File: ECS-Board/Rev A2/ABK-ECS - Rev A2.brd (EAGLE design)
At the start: 100 x 80 mm, 246 parts, among them J1 22-27-2061-06, J10 22-05-7068-06, J2 USB-B-S-RA, J3 1241050-5, J4 MSTBA2, J5 22-05-7068-06, J6 22-05-7028-02, J7 22-05-7068-06, J8 22-05-7068-06, J9 22-05-7028-02, K1 G6K-2G-Y, SW1 B3FS-1015, SW2 B3FS-1015, T1 EXMACHINA-LOGO-NAME, T10 MMBT2222AL, T11 MMBT2222AL, T12 IRLML5103TRPBF, T13 IRLML5103TRPBF, T14 IRLML5103TRPBF, T15 IRLML5103TRPBF, T16 MMBT2222AL, T17 MMBT2222AL, T18 MMBT2222AL, T19 MMBT2222AL, T2 IRLML5103TRPBF, T3 MMBT2222AL, T4 IRLML5103TRPBF, T5 IRLML5103TRPBF, T6 IRLML5103TRPBF, T7 IRLML5103TRPBF, T8 MMBT2222AL, T9 MMBT2222AL, U1 AT24C512C-SSHM-B, U2 LPC1768FBD100, U3 LT3686HDDPBF, U4 LT3686HDDPBF, U5 TC1264-3.3, U6 CD4050BD, U7 CD4050BD, X1 FC-135, X2 ASE-12, X3 3000

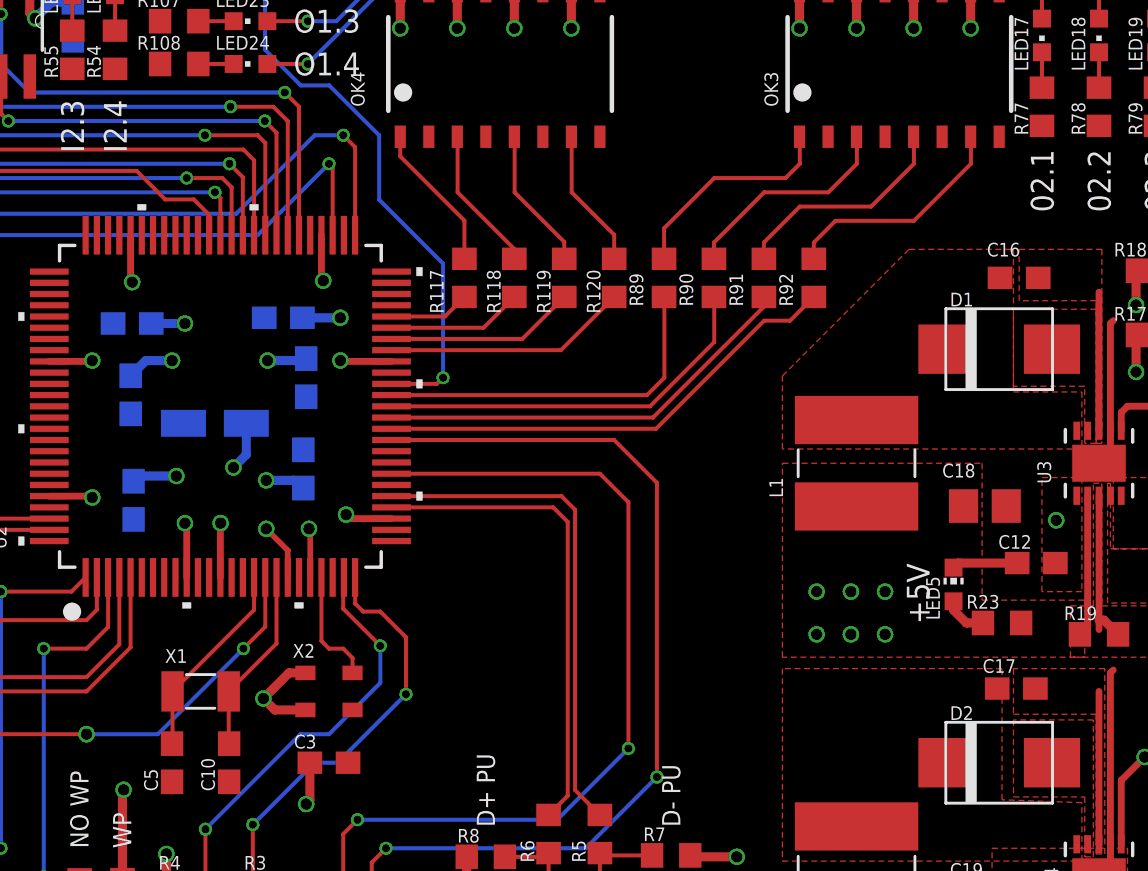
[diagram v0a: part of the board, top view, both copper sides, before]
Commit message: Minor route upgrade
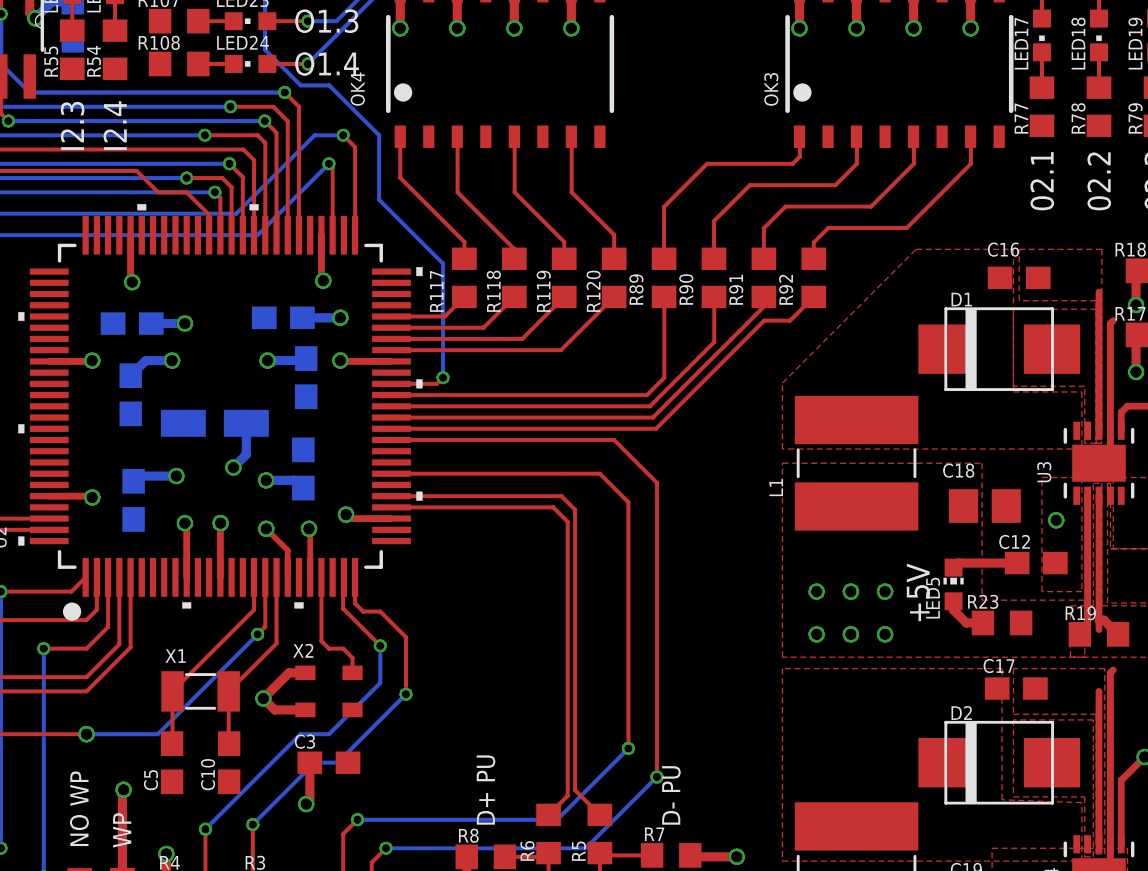
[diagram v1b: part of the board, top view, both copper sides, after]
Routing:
- net N$91: track 9.75 -> 10.3 mm
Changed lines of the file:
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@@
 <wire x1="13.55" y1="33.235" x2="16.815" y2="33.235" width="0.1778" layer="1"/>
 <wire x1="45.73" y1="26.03" x2="45.73" y2="23.835" width="0.1778" layer="1"/>
-<wire x1="45.73" y1="23.835" x2="44.755" y2="22.86" width="0.1778" layer="1"/>
-<via x="44.755" y="22.86" extent="1-16" drill="0.35"/>
-<wire x1="44.755" y1="22.86" x2="40.945" y2="19.05" width="0.1778" layer="16"/>
+<wire x1="45.73" y1="23.835" x2="45.39" y2="23.495" width="0.1778" layer="1"/>
+<via x="45.39" y="23.495" extent="1-16" drill="0.35"/>
+<wire x1="45.39" y1="23.495" x2="40.945" y2="19.05" width="0.1778" layer="16"/>
 <wire x1="40.945" y1="19.05" x2="37.77" y2="19.05" width="0.1778" layer="16"/>
 <via x="37.77" y="19.05" extent="1-16" drill="0.5"/>
@@
 <polygon width="0.3048" layer="1" rank="5">
 <vertex x="68.758" y="31.75"/>
-<vertex x="68.758" y="35.005"/>
-<vertex x="74.393" y="40.64"/>
+<vertex x="68.758" y="34.6875"/>
+<vertex x="74.7105" y="40.64"/>
 <vertex x="79.045" y="40.64"/>
 <vertex x="79.045" y="34.29"/>
@@
 <contactref element="OK3" pad="1"/>
 <contactref element="R89" pad="1"/>
-<wire x1="63.4875" y1="40.22" x2="63.4875" y2="41.58" width="0.1778" layer="1"/>
-<wire x1="63.4875" y1="41.58" x2="65.7225" y2="43.815" width="0.1778" layer="1"/>
-<wire x1="65.7225" y1="43.815" x2="68.8975" y2="43.815" width="0.1778" layer="1"/>
-<wire x1="68.8975" y1="43.815" x2="69.5325" y2="44.45" width="0.1778" layer="1"/>
-<wire x1="69.5325" y1="44.45" x2="69.5325" y2="45.6425" width="0.1778" layer="1"/>
+<wire x1="63.4875" y1="40.22" x2="63.4875" y2="42.5325" width="0.1778" layer="1"/>
+<wire x1="63.4875" y1="42.5325" x2="65.405" y2="44.45" width="0.1778" layer="1"/>
+<wire x1="65.405" y1="44.45" x2="69.215" y2="44.45" width="0.1778" layer="1"/>
+<wire x1="69.215" y1="44.45" x2="69.5325" y2="44.7675" width="0.1778" layer="1"/>
+<wire x1="69.5325" y1="44.7675" x2="69.5325" y2="45.6425" width="0.1778" layer="1"/>
 <wire x1="69.5325" y1="45.6425" x2="69.52" y2="45.655" width="0.1778" layer="1"/>
 </signal>
@@
 <contactref element="OK3" pad="3"/>
 <contactref element="R90" pad="1"/>
-<wire x1="65.71" y1="40.22" x2="65.71" y2="40.945" width="0.1778" layer="1"/>
-<wire x1="65.71" y1="40.945" x2="67.945" y2="43.18" width="0.1778" layer="1"/>
-<wire x1="67.945" y1="43.18" x2="70.8025" y2="43.18" width="0.1778" layer="1"/>
-<wire x1="70.8025" y1="43.18" x2="72.0725" y2="44.45" width="0.1778" layer="1"/>
+<wire x1="65.71" y1="40.22" x2="65.71" y2="41.8975" width="0.1778" layer="1"/>
+<wire x1="65.71" y1="41.8975" x2="67.31" y2="43.4975" width="0.1778" layer="1"/>
+<wire x1="67.31" y1="43.4975" x2="71.12" y2="43.4975" width="0.1778" layer="1"/>
+<wire x1="71.12" y1="43.4975" x2="72.0725" y2="44.45" width="0.1778" layer="1"/>
 <wire x1="72.0725" y1="44.45" x2="72.0725" y2="45.6425" width="0.1778" layer="1"/>
 <wire x1="72.0725" y1="45.6425" x2="72.06" y2="45.655" width="0.1778" layer="1"/>
@@
 <contactref element="OK3" pad="7"/>
 <wire x1="70.155" y1="40.22" x2="70.155" y2="40.945" width="0.1778" layer="1"/>
-<wire x1="70.155" y1="40.945" x2="71.12" y2="41.91" width="0.1778" layer="1"/>
-<wire x1="71.12" y1="41.91" x2="74.6125" y2="41.91" width="0.1778" layer="1"/>
-<wire x1="74.6125" y1="41.91" x2="77.1525" y2="44.45" width="0.1778" layer="1"/>
+<wire x1="70.155" y1="40.945" x2="70.8025" y2="41.5925" width="0.1778" layer="1"/>
+<wire x1="70.8025" y1="41.5925" x2="74.295" y2="41.5925" width="0.1778" layer="1"/>
+<wire x1="74.295" y1="41.5925" x2="77.1525" y2="44.45" width="0.1778" layer="1"/>
 <wire x1="77.1525" y1="44.45" x2="77.1525" y2="45.6425" width="0.1778" layer="1"/>
 <wire x1="77.1525" y1="45.6425" x2="77.14" y2="45.655" width="0.1778" layer="1"/>
@@
 <contactref element="OK3" pad="5"/>
 <contactref element="R91" pad="1"/>
-<wire x1="67.9325" y1="40.22" x2="67.9325" y2="40.945" width="0.1778" layer="1"/>
-<wire x1="67.9325" y1="40.945" x2="69.5325" y2="42.545" width="0.1778" layer="1"/>
-<wire x1="69.5325" y1="42.545" x2="72.7075" y2="42.545" width="0.1778" layer="1"/>
+<wire x1="67.9325" y1="40.22" x2="67.9325" y2="41.58" width="0.1778" layer="1"/>
+<wire x1="67.9325" y1="41.58" x2="68.8975" y2="42.545" width="0.1778" layer="1"/>
+<wire x1="68.8975" y1="42.545" x2="72.7075" y2="42.545" width="0.1778" layer="1"/>
 <wire x1="72.7075" y1="42.545" x2="74.6125" y2="44.45" width="0.1778" layer="1"/>
 <wire x1="74.6125" y1="44.45" x2="74.6125" y2="45.6425" width="0.1778" layer="1"/>
@@
 <contactref element="OK4" pad="1"/>
 <contactref element="R117" pad="1"/>
-<wire x1="54.5975" y1="40.22" x2="54.5975" y2="41.9225" width="0.1778" layer="1"/>
-<wire x1="54.5975" y1="41.9225" x2="51.74" y2="44.78" width="0.1778" layer="1"/>
-<wire x1="51.74" y1="44.78" x2="51.74" y2="45.655" width="0.1778" layer="1"/>
+<wire x1="54.5975" y1="40.22" x2="54.5975" y2="40.97" width="0.1778" layer="1"/>
+<wire x1="54.5975" y1="40.97" x2="51.74" y2="43.8275" width="0.1778" layer="1"/>
+<wire x1="51.74" y1="43.8275" x2="51.74" y2="45.655" width="0.1778" layer="1"/>
 </signal>
 <signal name="N$42">
@@
 <contactref element="U2" pad="64"/>
 <wire x1="43.23" y1="41.27" x2="43.23" y2="42.1775" width="0.1778" layer="1"/>
-<wire x1="43.23" y1="42.1775" x2="42.545" y2="42.8625" width="0.1778" layer="1"/>
-<wire x1="42.545" y1="42.8625" x2="41.275" y2="42.8625" width="0.1778" layer="1"/>
-<wire x1="41.275" y1="42.8625" x2="40.005" y2="44.1325" width="0.1778" layer="1"/>
+<wire x1="43.23" y1="42.1775" x2="42.2275" y2="43.18" width="0.1778" layer="1"/>
+<wire x1="42.2275" y1="43.18" x2="40.9575" y2="43.18" width="0.1778" layer="1"/>
+<wire x1="40.9575" y1="43.18" x2="40.005" y2="44.1325" width="0.1778" layer="1"/>
 <wire x1="40.005" y1="44.1325" x2="10.16" y2="44.1325" width="0.1778" layer="1"/>
 <wire x1="10.16" y1="44.1325" x2="9.2075" y2="45.085" width="0.1778" layer="1"/>

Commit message: Generate Gerber and MDP files
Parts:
- LED21: value 01.1 -> Blue
- LED5, LED6: device led:CHIP-LED0603 -> led:CHIPLED_0603
- R1: value 4K7 -> 4K7, DNI
- R10: value 0R -> 10K
- R101, R64, R73: value 100 -> 330
- R105, R40, R77: value 1K5 -> 100
- R109, R81: value 4K7 -> 1K5
- R113, R85: value 1K -> 4K7
- R117, R89: value 330 -> 1K
- R12: value 10K -> 0R
- R121: value 0R -> 330
- R13, R23: value 1K5 -> 10K
- R15: value 31K6 -> 1K5
- R17: value 4K7 -> 31K6
- R19: value 52K3 -> 4K7
- R20: value 10K -> 52K3
- R21: value 31K6 -> 10K
- R22: value 10K -> 31K6
- R25: value 100 -> 1K5
- R26: value 1K -> 100
- R34, R49: value 4K7 -> 1K
- R39: value 100 -> 4K7
- R41: value 1K -> 1K5
- R5: value 33 -> 0R
- R53: value 1K5 -> 4K7
- R62: value 10K -> 1K5
- R63, R69, R97: value 330 -> 10K
- R65: value 10K -> 100
- R7: value 1K5 -> 33
- R8: value 1K5 -> 1K5, DNI
- R9: value 10K -> 1K5, DNI
- R93: value 10K -> 330
- moved R41 73.4 mm to (90.5, 55.2), turned to 180 degrees
- moved R38 72.6 mm to (22.5, 57.1)
- moved R25 63.6 mm to (78.6, 5.78), turned to 0 degrees
- moved R26 53.4 mm to (88.6, 68.6), turned to 180 degrees
- moved R9 48.0 mm to (55.5, 13.6)
- moved R62 47.4 mm to (4.13, 49.5), flipped to the top, turned to 270 degrees
- moved R15 45.7 mm to (46.4, 7.62), turned to 90 degrees
- moved R5 44.1 mm to (20.3, 32.4), turned to 270 degrees
- moved R13 43.1 mm to (16.8, 32.4), turned to 270 degrees
- moved R121 41.5 mm to (61.3, 39.4)
- moved R93 36.8 mm to (70.2, 39.4), flipped to the top, turned to 270 degrees
- moved R53 35.9 mm to (6.03, 57.1), turned to 90 degrees
- moved R65 27.5 mm to (44.5, 59.1), flipped to the top, turned to 270 degrees
- moved R17 26.1 mm to (86.7, 10.8)
- moved R81 23.6 mm to (87.9, 47.0), turned to 270 degrees
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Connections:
- net !RESET: now also R13.1; no longer R12.1
- net +24V: now also R101.2, R19.2, R64.2, R73.2; no longer R17.2, R63.2, R69.2, R97.2
- net +3V3: now also R10.2, R13.2, R22.2, R25.2, R9.1; no longer R12.2, R21.2, R24.2, R7.1, R9.2
- net +5V: now also R20.2, R24.2, R39.1, R41.2; no longer R19.2, R23.2, R38.1, R40.2
- net BOOT_SELECT_P2_10: now also R11.1, R5.1; no longer R10.1, R121.1
- net BOOT_SELECT_P2_12: now also R12.1; no longer R11.1
- net GND: now also R113.2, R15.2, R17.1, R21.1, R23.1, R38.2, R62.2, R63.1, R69.1, R85.2, R97.1; no longer R105.2, R13.2, R15.1, R20.1, R22.1, R34.2, R49.2, R62.1, R65.1, R77.2, R93.1
- net INPUT1.1: now also R49.2, R53.1; no longer R48.2, R52.1
- net INPUT1.2: now also R48.2, R52.1; no longer R47.2, R51.1
- net INPUT1.3: now also R47.2, R51.1; no longer R46.2, R50.1
- net INPUT1.4: now also R46.2, R50.1; no longer R45.2, R49.1
- net INPUT2.1: now also R34.2, R38.1; no longer R33.2, R37.1
- net INPUT2.2: now also R33.2, R37.1; no longer R32.2, R36.1
- net INPUT2.3: now also R32.2, R36.1; no longer R31.2, R35.1
- net INPUT2.4: now also R31.2, R35.1; no longer R30.2, R34.1
- net INPUT3.1: now also R40.2; no longer R39.2
- net ISP_RTS: now also R5.2; no longer R121.2
- net MOTOR_VFQ: now also R63.2; no longer R62.2
- net N$1: now also R7.1, R9.2; no longer R6.1, R8.2
- net N$100: now also R46.1; no longer R45.1
- net N$101: now also R43.2; no longer R42.2
- net N$102: now also R43.1; no longer R42.1
- net N$103: now also R47.1; no longer R46.1
- net N$104: now also R44.2; no longer R43.2
- net N$105: now also R44.1; no longer R43.1
- net N$106: now also R48.1; no longer R47.1
- net N$107: now also R59.1; no longer R58.1
- net N$108: now also R60.1; no longer R59.1
- net N$109: now also R61.1; no longer R60.1
- net N$110: now also R49.1; no longer R48.1
- net N$111: now also R45.2; no longer R44.2
- net N$112: now also R45.1; no longer R44.1
- net N$13: now also R22.1, R23.2; no longer R21.1, R22.2
- net N$17: now also R74.2; no longer R73.2
- net N$18: now also R70.1; no longer R69.1
- net N$19: now also R75.2; no longer R74.2
- net N$2: now also R6.1, R8.2; no longer R5.1, R7.2
- net N$20: now also R71.1; no longer R70.1
- net N$21: now also R76.2; no longer R75.2
- net N$22: now also R72.1; no longer R71.1
- net N$23: now also R77.2; no longer R76.2
- net N$24: now also R73.1; no longer R72.1
- net N$25: now also R65.1; no longer R64.1
- net N$26: now also R64.1; no longer R63.1
- net N$28: now also R26.2; no longer R25.2
- net N$29: now also R14.1; no longer R13.1
- net N$3: now also R15.1; no longer R14.1
- net N$31: now also R102.1, R110.1, R114.1; no longer R101.1, R109.1, R113.1
- net N$32: now also R26.1; no longer R25.1
- net N$33: now also R114.2; no longer R113.2
- net N$34: now also R103.1, R111.1, R115.1; no longer R102.1, R110.1, R114.1
- net N$35: now also R115.2; no longer R114.2
- net N$36: now also R104.1, R112.1, R116.1; no longer R103.1, R111.1, R115.1
- net N$37: now also R105.1, R113.1, R117.1; no longer R104.1, R112.1, R116.1
- net N$38: now also R116.2; no longer R115.2
- net N$39: now also R117.2; no longer R116.2
- net N$4: now also R16.2; no longer R15.2
- net N$40: now also R118.1; no longer R117.1
- net N$41: now also R27.2; no longer R26.2
- net N$42: now also R119.1; no longer R118.1
- net N$43: now also R121.1; no longer R120.1
- net N$44: now also R19.1; no longer R18.1
- net N$45: now also R18.1; no longer R17.1
- net N$46: now also R120.1; no longer R119.1
- net N$47: now also R28.2; no longer R27.2
- net N$48: now also R29.2; no longer R28.2
- net N$49: now also R30.2; no longer R29.2
- net N$5: now also R10.1, R12.2; no longer R10.2, R9.1
- net N$50: now also R25.1; no longer R24.1
- net N$51: now also R24.1; no longer R23.1
- net N$52: now also R30.1; no longer R29.1
- net N$53: now also R29.1; no longer R28.1
- net N$54: now also R28.1; no longer R27.1
- net N$55: now also R27.1; no longer R26.1
- net N$56: now also R54.1; no longer R53.1
- net N$57: now also R55.1; no longer R54.1
- net N$58: now also R56.1; no longer R55.1
- net N$59: now also R57.1; no longer R56.1
- net N$61: now also R34.1; no longer R33.1
- net N$62: now also R33.1; no longer R32.1
- net N$63: now also R32.1; no longer R31.1
- net N$64: now also R31.1; no longer R30.1
- net N$65: now also R58.1; no longer R57.1
- net N$66: now also R106.1; no longer R105.1
- net N$67: now also R107.1; no longer R106.1
- net N$68: now also R108.1; no longer R107.1
- net N$69: now also R109.1; no longer R108.1
- net N$7: now also R17.2; no longer R16.2
- net N$71: now also R98.1; no longer R97.1
- net N$72: now also R99.1; no longer R98.1
- net N$73: now also R39.2, R40.1; no longer R38.2, R39.1
- net N$74: now also R41.1; no longer R40.1
- net N$75: now also R74.1, R82.1, R86.1; no longer R73.1, R81.1, R85.1
- net N$76: now also R86.2; no longer R85.2
- net N$77: now also R100.1; no longer R99.1
- net N$78: now also R101.1; no longer R100.1
- net N$79: now also R75.1, R83.1, R87.1; no longer R74.1, R82.1, R86.1
- net N$80: now also R87.2; no longer R86.2
- net N$81: now also R42.2; no longer R41.2
- net N$82: now also R42.1; no longer R41.1
- net N$83: now also R76.1, R84.1, R88.1; no longer R75.1, R83.1, R87.1
- net N$84: now also R102.2; no longer R101.2
- net N$85: now also R103.2; no longer R102.2
- net N$86: now also R77.1, R85.1, R89.1; no longer R76.1, R84.1, R88.1
- net N$87: now also R88.2; no longer R87.2
- net N$88: now also R89.2; no longer R88.2
- net N$89: now also R90.1; no longer R89.1
- net N$9: now also R20.1, R21.2; no longer R19.1, R20.2
- net N$90: now also R62.1; no longer R61.1
- net N$91: now also R91.1; no longer R90.1
- net N$92: now also R93.1; no longer R92.1
- net N$93: now also R92.1; no longer R91.1
- net N$94: now also R78.1; no longer R77.1
- net N$95: now also R79.1; no longer R78.1
- net N$96: now also R80.1; no longer R79.1
- net N$97: now also R81.1; no longer R80.1
- net N$98: now also R104.2; no longer R103.2
- net N$99: now also R105.2; no longer R104.2
- net OUTPUT1.1: now also R94.2; no longer R93.2
- net OUTPUT1.1_MCU: now also R118.2; no longer R117.2
- net OUTPUT1.2: now also R95.2; no longer R94.2
- net OUTPUT1.2_MCU: now also R119.2; no longer R118.2
- net OUTPUT1.3: now also R96.2; no longer R95.2
- net OUTPUT1.3_MCU: now also R120.2; no longer R119.2
- net OUTPUT1.4: now also R97.2; no longer R96.2
- net OUTPUT1.4_MCU: now also R121.2; no longer R120.2
- net OUTPUT2.1: now also R66.2; no longer R65.2
- net OUTPUT2.1_MCU: now also R90.2; no longer R89.2
- net OUTPUT2.2: now also R67.2; no longer R66.2
- net OUTPUT2.2_MCU: now also R91.2; no longer R90.2
- net OUTPUT2.3: now also R68.2; no longer R67.2
- net OUTPUT2.3_MCU: now also R92.2; no longer R91.2
- net OUTPUT2.4: now also R69.2; no longer R68.2
- net OUTPUT2.4_MCU: now also R93.2; no longer R92.2
- net OUTPUT3.2_MCU: now also R65.2; no longer R64.2
- net USB_D_N: now also R6.2; no longer R5.2
- net USB_D_P: now also R7.2; no longer R6.2

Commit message: Replace output resistance and fuse LED
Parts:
- R100, R101, R64, R70, R71, R72, R73, R98, R99: value 330 -> 10K
- R102, R103, R104, R105, R74, R75, R76, R77: value 100 -> 1K
- R114, R115, R116, R117, R86, R87, R88, R89: value 1K -> 100
